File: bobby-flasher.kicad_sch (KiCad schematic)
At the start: 28 parts, among them J1 Conn_01x03, J2 Conn_01x06, J3 Flash, Q1 SS8050_C2150, Q2 SS8050_C2150, U1 CH343G, U2 AMS1117-3.3

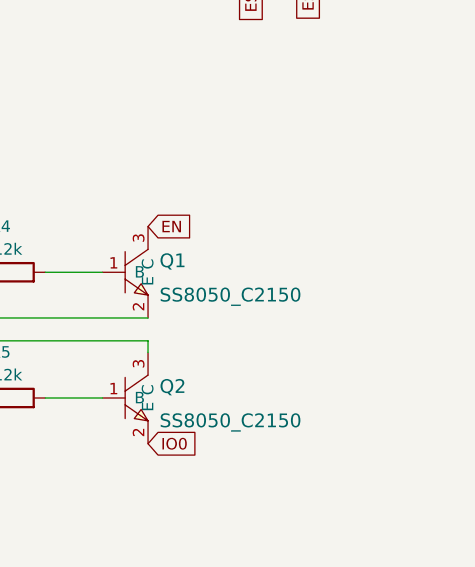
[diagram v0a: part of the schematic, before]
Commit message: peters fixes, resistor on DTR missing
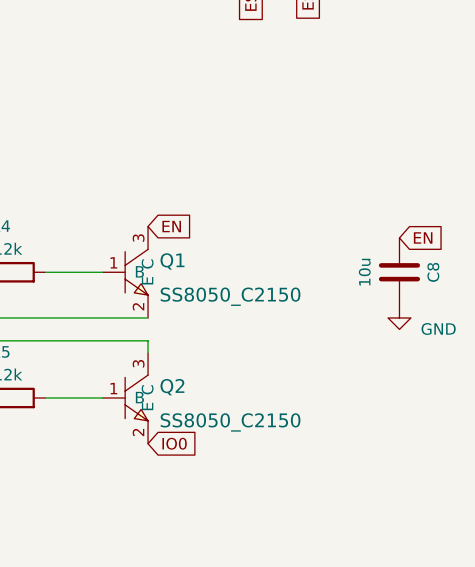
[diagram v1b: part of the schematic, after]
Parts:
- added C8: 10u, Capacitor_SMD:C_0603_1608Metric, symbol Device:C
- C2, C5: LCSC Part # C19702 -> C96446
- Q1, Q2: footprint SS8050:SOT-23-3_L2.9-W1.3-P1.90-LS2.4-BR -> Package_TO_SOT_SMD:SOT-23
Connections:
- net EN: now also C8.2
- net GND: now also C8.1
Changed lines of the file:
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@@
+    )
+  )
+  (global_label "EN" (shape input) (at 205.74 133.35 0) (fields_autoplaced)
+    (effects (font (size 1.27 1.27)) (justify left))
+    (property "Referenzen zwischen Schaltplänen" "${INTERSHEET_REFS}" (id 0) (at 210.6326 133.2706 0)
+      (effects (font (size 1.27 1.27)) (justify left) hide)
     )
   )
@@
       (effects (font (size 1.524 1.524)) (justify left))
     )
-    (property "Footprint" "SS8050:SOT-23-3_L2.9-W1.3-P1.90-LS2.4-BR" (id 2) (at 177.8 149.86 0)
+    (property "Footprint" "Package_TO_SOT_SMD:SOT-23" (id 2) (at 177.8 149.86 0)
       (effects (font (size 1.524 1.524)) hide)
     )
@@
       (effects (font (size 1.524 1.524)) (justify left))
     )
-    (property "Footprint" "SS8050:SOT-23-3_L2.9-W1.3-P1.90-LS2.4-BR" (id 2) (at 177.8 163.83 0)
+    (property "Footprint" "Package_TO_SOT_SMD:SOT-23" (id 2) (at 177.8 163.83 0)
       (effects (font (size 1.524 1.524)) hide)
     )
@@
     (pin "1")
   )
+  (symbol (lib_id "power:GND") (at 205.74 140.97 0) (unit 1)
+    (in_bom yes) (on_board yes)
+    (property "Reference" "#PWR0134" (id 0) (at 205.74 147.32 0)
+      (effects (font (size 1.27 1.27)) hide)
+    )
+    (property "Value" "GND" (id 1) (at 212.09 143.51 0)
+      (effects (font (size 1.27 1.27)) (justify right))
+    )
+    (property "Footprint" "" (id 2) (at 205.74 140.97 0)
+      (effects (font (size 1.27 1.27)) hide)
+    )
+    (property "Datasheet" "" (id 3) (at 205.74 140.97 0)
+      (effects (font (size 1.27 1.27)) hide)
+    )
+    (pin "1")
+  )
   (symbol (lib_id "Device:C") (at 105.41 180.34 180) (unit 1)
     (in_bom yes) (on_board yes)
@@
       (effects (font (size 1.27 1.27)) hide)
     )
-    (property "LCSC Part #" "C19702" (id 4) (at 105.41 180.34 90)
+    (property "LCSC Part #" "C96446" (id 4) (at 105.41 180.34 90)
       (effects (font (size 1.27 1.27)) hide)
     )
@@
     (pin "1")
   )
+  (symbol (lib_id "Device:C") (at 205.74 137.16 180) (unit 1)
+    (in_bom yes) (on_board yes)
+    (property "Reference" "C8" (id 0) (at 209.55 137.16 90))
+    (property "Value" "10u" (id 1) (at 201.93 137.16 90))
+    (property "Footprint" "Capacitor_SMD:C_0603_1608Metric" (id 2) (at 204.7748 133.35 0)
+      (effects (font (size 1.27 1.27)) hide)
+    )
+    (property "Datasheet" "~" (id 3) (at 205.74 137.16 0)
+      (effects (font (size 1.27 1.27)) hide)
+    )
+    (property "LCSC Part #" "C96446" (id 4) (at 205.74 137.16 90)
+      (effects (font (size 1.27 1.27)) hide)
+    )
+    (pin "1")
+    (pin "2")
+  )
   (symbol (lib_id "power:+5V") (at 166.37 85.09 0) (unit 1)
     (in_bom yes) (on_board yes)
@@
       (effects (font (size 1.27 1.27)) hide)
     )
-    (property "LCSC Part #" "C19702" (id 4) (at 135.89 180.34 90)
+    (property "LCSC Part #" "C96446" (id 4) (at 135.89 180.34 90)
       (effects (font (size 1.27 1.27)) hide)
     )
@@
       (reference "#PWR0133") (unit 1) (value "+3.3V") (footprint "")
     )
+    (path "/c89cd0b5-1afd-42d5-aaca-65bb60ffd5b8"
+      (reference "#PWR0134") (unit 1) (value "GND") (footprint "")
+    )
     (path "/34194ef4-e853-4693-8338-89bc6f8fe21a"
       (reference "C1") (unit 1) (value "100n") (footprint "Capacitor_SMD:C_0402_1005Metric")
@@
       (reference "C7") (unit 1) (value "1u") (footprint "Capacitor_SMD:C_0603_1608Metric")
     )
+    (path "/e4f0b19b-5c3e-4326-b844-19ce566527d6"
+      (reference "C8") (unit 1) (value "10u") (footprint "Capacitor_SMD:C_0603_1608Metric")
+    )
     (path "/446d393f-e711-4111-885c-286518d34313"
       (reference "D1") (unit 1) (value "LED") (footprint "LED_SMD:LED_0603_1608Metric")
@@
     )
     (path "/167678fc-2cfb-4499-b87a-2db93b2d7d52"
-      (reference "Q1") (unit 1) (value "SS8050_C2150") (footprint "SS8050:SOT-23-3_L2.9-W1.3-P1.90-LS2.4-BR")
+      (reference "Q1") (unit 1) (value "SS8050_C2150") (footprint "Package_TO_SOT_SMD:SOT-23")
     )
     (path "/6a08af6d-27e8-4b9d-9e93-5ff688fd1a61"
-      (reference "Q2") (unit 1) (value "SS8050_C2150") (footprint "SS8050:SOT-23-3_L2.9-W1.3-P1.90-LS2.4-BR")
+      (reference "Q2") (unit 1) (value "SS8050_C2150") (footprint "Package_TO_SOT_SMD:SOT-23")
     )
     (path "/950ef4f1-7011-4ed7-a70f-4ae2249893a7"

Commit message: fixed version
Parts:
- added R10: 10k, Resistor_SMD:R_0402_1005Metric, symbol Device:R
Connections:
- net +3V3: now also R10.2
- net DTR: now also Q2.2 (E), R10.1; no longer Q2.3 (C)
- net IO0: now also Q2.3 (C); no longer Q2.2 (E)
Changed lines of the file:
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@@
+    (stroke (width 0) (type default) (color 0 0 0 0))
+  )
+  (wire (pts (xy 152.4 162.56) (xy 154.94 162.56))
+    (stroke (width 0) (type default) (color 0 0 0 0))
+  )
+  (wire (pts (xy 142.24 162.56) (xy 144.78 162.56))
     (stroke (width 0) (type default) (color 0 0 0 0))
   )
@@
     (effects (font (size 1.27 1.27)) (justify right))
     (property "Referenzen zwischen Schaltplänen" "${INTERSHEET_REFS}" (id 0) (at 34.9612 90.0906 0)
+      (effects (font (size 1.27 1.27)) (justify right) hide)
+    )
+  )
+  (global_label "DTR" (shape input) (at 142.24 162.56 180) (fields_autoplaced)
+    (effects (font (size 1.27 1.27)) (justify right))
+    (property "Referenzen zwischen Schaltplänen" "${INTERSHEET_REFS}" (id 0) (at 136.3193 162.6394 0)
       (effects (font (size 1.27 1.27)) (justify right) hide)
     )
@@
     (pin "1")
   )
+  (symbol (lib_id "power:+3.3V") (at 154.94 162.56 0) (unit 1)
+    (in_bom yes) (on_board yes)
+    (property "Reference" "#PWR0135" (id 0) (at 154.94 166.37 0)
+      (effects (font (size 1.27 1.27)) hide)
+    )
+    (property "Value" "+3.3V" (id 1) (at 154.94 158.75 0))
+    (property "Footprint" "" (id 2) (at 154.94 162.56 0)
+      (effects (font (size 1.27 1.27)) hide)
+    )
+    (property "Datasheet" "" (id 3) (at 154.94 162.56 0)
+      (effects (font (size 1.27 1.27)) hide)
+    )
+    (pin "1")
+  )
   (symbol (lib_id "power:+5V") (at 36.83 162.56 90) (unit 1)
     (in_bom yes) (on_board yes)
@@
     (pin "1")
   )
-  (symbol (lib_id "SS8050:SS8050_C2150") (at 177.8 151.13 0) (unit 1)
-    (in_bom yes) (on_board yes) (fields_autoplaced)
-    (property "Reference" "Q2" (id 0) (at 179.07 149.86 0)
+  (symbol (lib_id "Device:R") (at 148.59 162.56 90) (unit 1)
+    (in_bom yes) (on_board yes)
+    (property "Reference" "R10" (id 0) (at 148.59 157.48 90)
+      (effects (font (size 1.27 1.27)) (justify left))
+    )
+    (property "Value" "10k" (id 1) (at 149.86 160.02 90)
+      (effects (font (size 1.27 1.27)) (justify left))
+    )
+    (property "Footprint" "Resistor_SMD:R_0402_1005Metric" (id 2) (at 148.59 164.338 90)
+      (effects (font (size 1.27 1.27)) hide)
+    )
+    (property "Datasheet" "~" (id 3) (at 148.59 162.56 0)
+      (effects (font (size 1.27 1.27)) hide)
+    )
+    (property "LCSC" "C25744" (id 4) (at 148.59 162.56 90)
+      (effects (font (size 1.27 1.27)) hide)
+    )
+    (pin "1")
+    (pin "2")
+  )
+  (symbol (lib_id "SS8050:SS8050_C2150") (at 177.8 151.13 0) (mirror x) (unit 1)
+    (in_bom yes) (on_board yes) (fields_autoplaced)
+    (property "Reference" "Q2" (id 0) (at 178.435 150.0653 0)
       (effects (font (size 1.524 1.524)) (justify left))
     )
-    (property "Value" "SS8050_C2150" (id 1) (at 179.07 153.67 0)
+    (property "Value" "SS8050_C2150" (id 1) (at 178.435 153.3443 0)
       (effects (font (size 1.524 1.524)) (justify left))
     )
-    (property "Footprint" "Package_TO_SOT_SMD:SOT-23" (id 2) (at 177.8 163.83 0)
+    (property "Footprint" "Package_TO_SOT_SMD:SOT-23" (id 2) (at 177.8 138.43 0)
       (effects (font (size 1.524 1.524)) hide)
     )
-    (property "Datasheet" "https://lcsc.com/product-detail/Transistors-NPN-PNP_SS8050-Y1-200-350_C2150.html" (id 3) (at 177.8 168.91 0)
+    (property "Datasheet" "https://lcsc.com/product-detail/Transistors-NPN-PNP_SS8050-Y1-200-350_C2150.html" (id 3) (at 177.8 133.35 0)
       (effects (font (size 1.524 1.524)) hide)
     )
@@
       (reference "#PWR0134") (unit 1) (value "GND") (footprint "")
     )
+    (path "/4f9fdeff-02c1-41f0-9d31-f5f8315f0ae5"
+      (reference "#PWR0135") (unit 1) (value "+3.3V") (footprint "")
+    )
     (path "/34194ef4-e853-4693-8338-89bc6f8fe21a"
       (reference "C1") (unit 1) (value "100n") (footprint "Capacitor_SMD:C_0402_1005Metric")
@@
       (reference "R9") (unit 1) (value "1k") (footprint "Resistor_SMD:R_0402_1005Metric")
     )
+    (path "/63e59f98-801c-4ba0-a31f-3c2327708cfc"
+      (reference "R10") (unit 1) (value "10k") (footprint "Resistor_SMD:R_0402_1005Metric")
+    )
     (path "/ae033daf-360c-4132-9495-c228de33337f"
